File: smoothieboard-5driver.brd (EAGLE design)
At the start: 129.5 x 105.1 mm, 253 parts, among them IC1 LPC1769, IC10 LM1117-3.3V, IC11 78L12F, IC12 A4982, IC2 A4982, IC3 A4982, IC4 MCP44X1, IC5 A4982, IC6 A4982, IC9 MCP44X1, J10 POWER_JACKSMD, Q1 BSL207SP, Q2 12MHz, Q3 25MHz, Q6 AOT240L, Q7 AOT240L, Q8 ZXMN4A06GTA, Q9 ZXMN4A06GTA, U1 USD-SOCKETNEW, X14 USBPTH

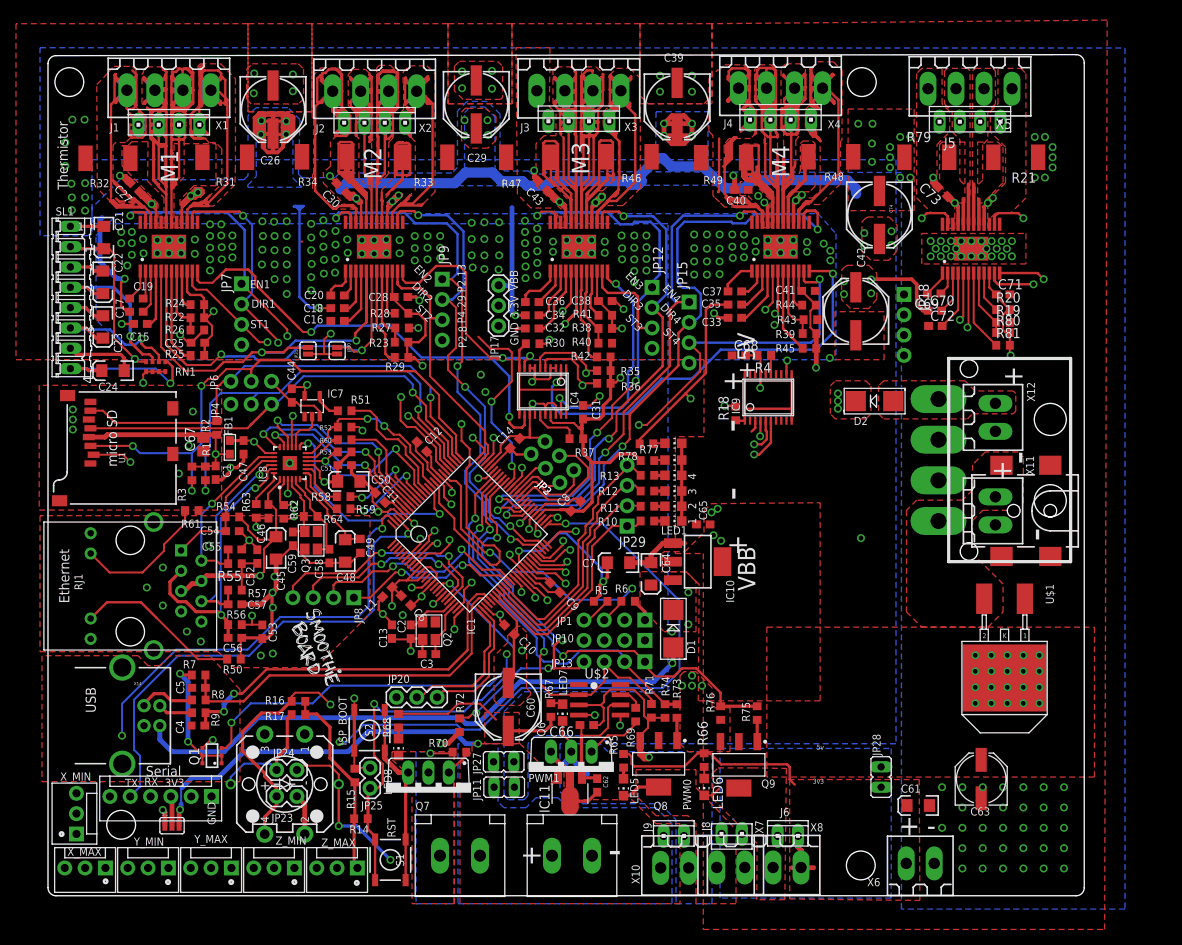
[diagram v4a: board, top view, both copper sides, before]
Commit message: remove VBB poly supplying mosfet drivers from bottom of board to improve driver heatsinking, VBB poly on route15 is adequate.
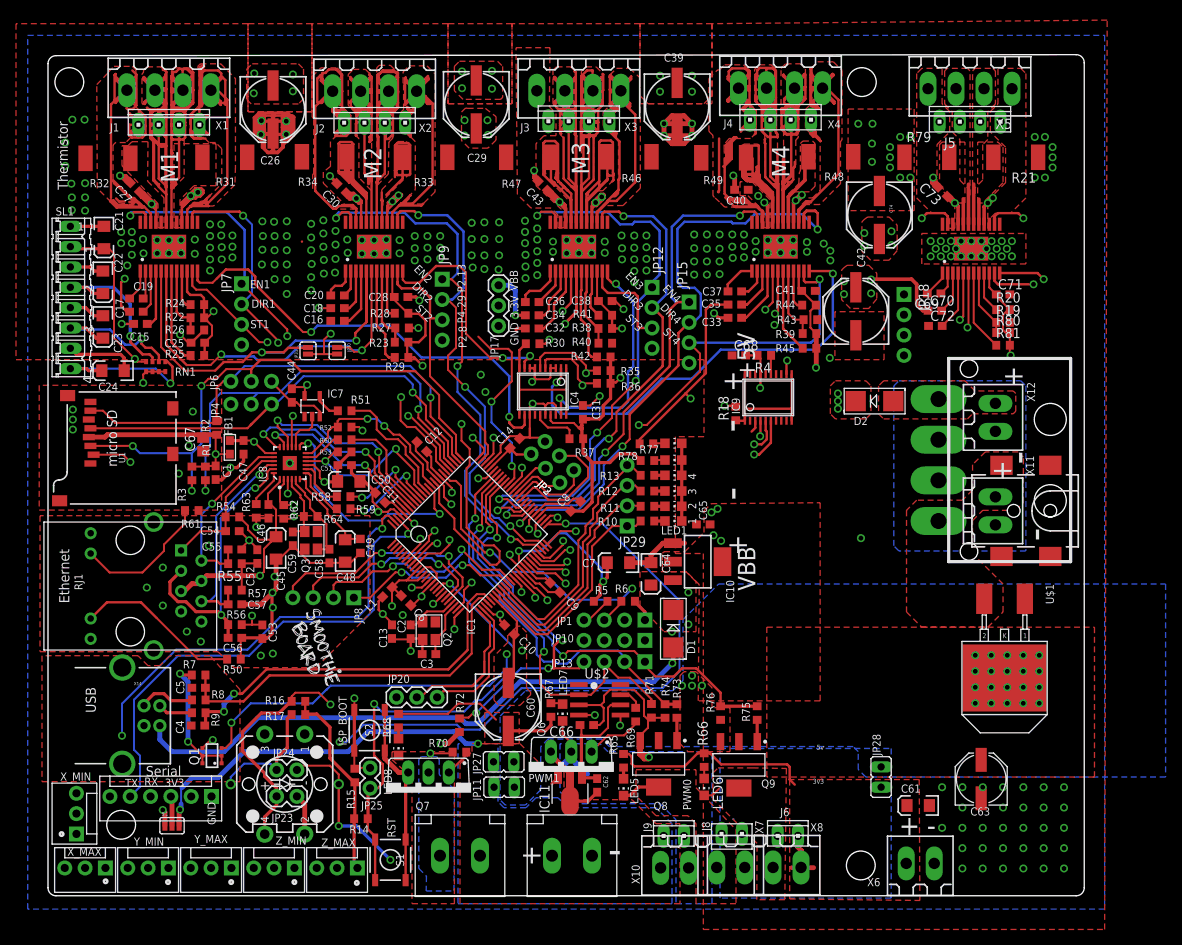
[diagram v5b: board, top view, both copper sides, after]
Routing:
- net VBB: track 351.1 -> 276.3 mm

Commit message: Gave small mosfets more heatsink area, moved some signal traces from bottom layer to route15 to improve stepper driver cooling, lots of other tweaks
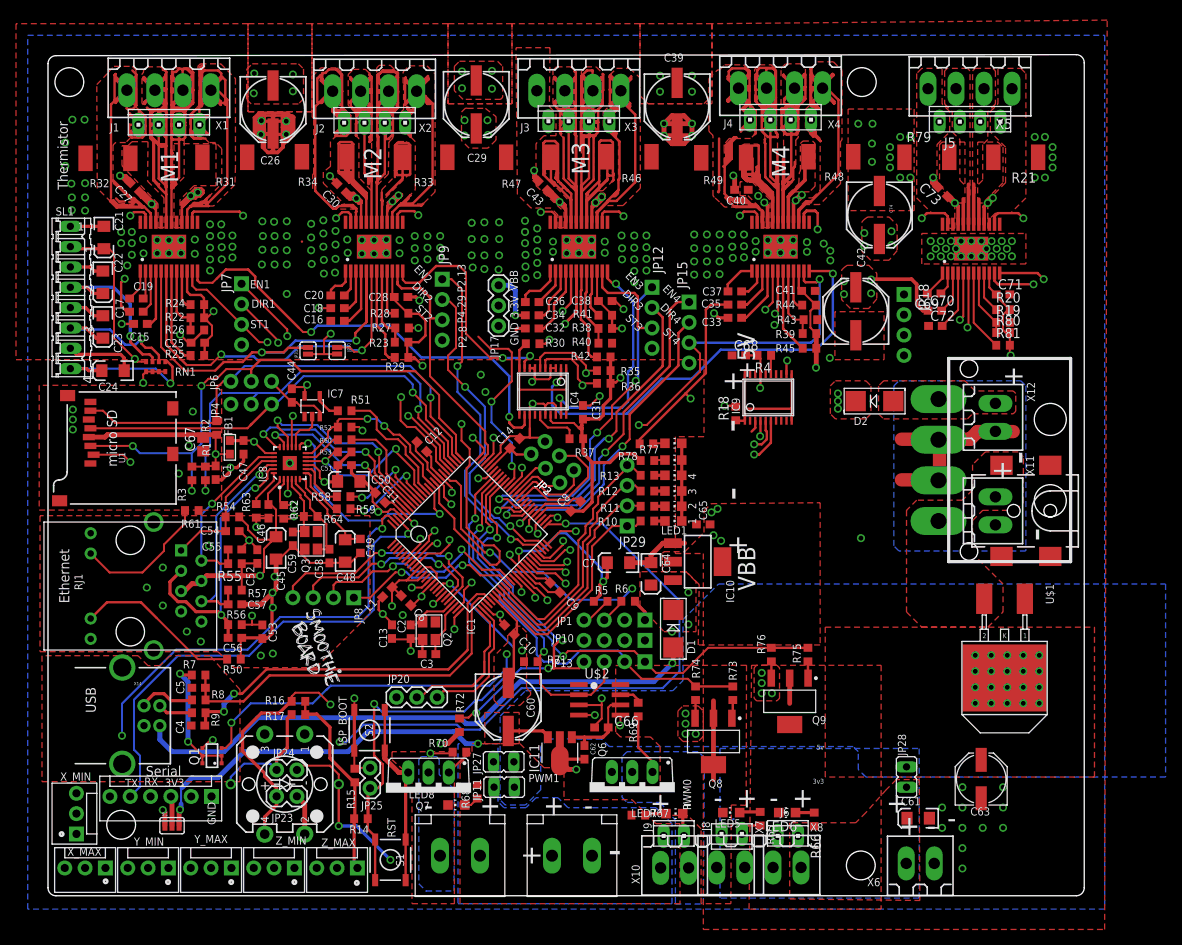
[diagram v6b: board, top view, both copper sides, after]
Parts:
- moved LED7 18.8 mm to (78.3, 9.40), turned to 270 degrees
- moved R65 18.6 mm to (89.0, 8.76), turned to 90 degrees
- moved R67 17.1 mm to (73.8, 9.21), turned to 0 degrees
- moved R71 16.3 mm to (60.4, 28.4), turned to 0 degrees
- moved R66 15.6 mm to (95.8, 8.68), turned to 90 degrees
- moved LED5 13.8 mm to (85.4, 9.53), turned to 90 degrees
- moved R68 13.3 mm to (53.7, 12.1)
- moved LED6 10.9 mm to (92.4, 9.53), turned to 90 degrees
- moved LED8 10.2 mm to (51.1, 10.5), turned to 90 degrees
- moved Q9 10.2 mm to (92.7, 23.4)
- moved R76 9.68 mm to (90.4, 29.3)
- moved R75 9.68 mm to (95.0, 29.3)
- moved Q6 8.03 mm to (73.0, 12.1)
- moved Q8 7.41 mm to (83.2, 18.4)
- moved R73 7.33 mm to (85.6, 24.4)
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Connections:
- net N$18 renamed SMALL_MOSFET_POWER
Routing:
- net SMALL_MOSFET_POWER: track 32.8 -> 3.04 mm
- net 5V: track 109.4 -> 129.7 mm
- net MOSFET_DRIVE: track 21.3 -> 5.38 mm
- net N$92: track 11.0 -> 2.86 mm
- net PWM1: track 51.5 -> 43.5 mm
- net 12VREG: track 16.6 -> 10.6 mm
- net PWM0: track 49.5 -> 55.4 mm
- net N$88: track 5.34 -> 9.84 mm
- net P2.6: track 58.0 -> 61.6 mm
- net GND: track 264.9 -> 268.1 mm, vias 300 -> 281
- net N$18: track 2.23 -> 3.81 mm
- net EN3: track 71.2 -> 70.0 mm
- net N$81: track 1.40 -> 2.61 mm
- net N$105: track 1.51 -> 2.69 mm
- net PW5: track 46.1 -> 47.2 mm
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- removed copper zone on layer 15, net 5V

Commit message: Added a bunch of ground stitching vias, also some routing tweaks
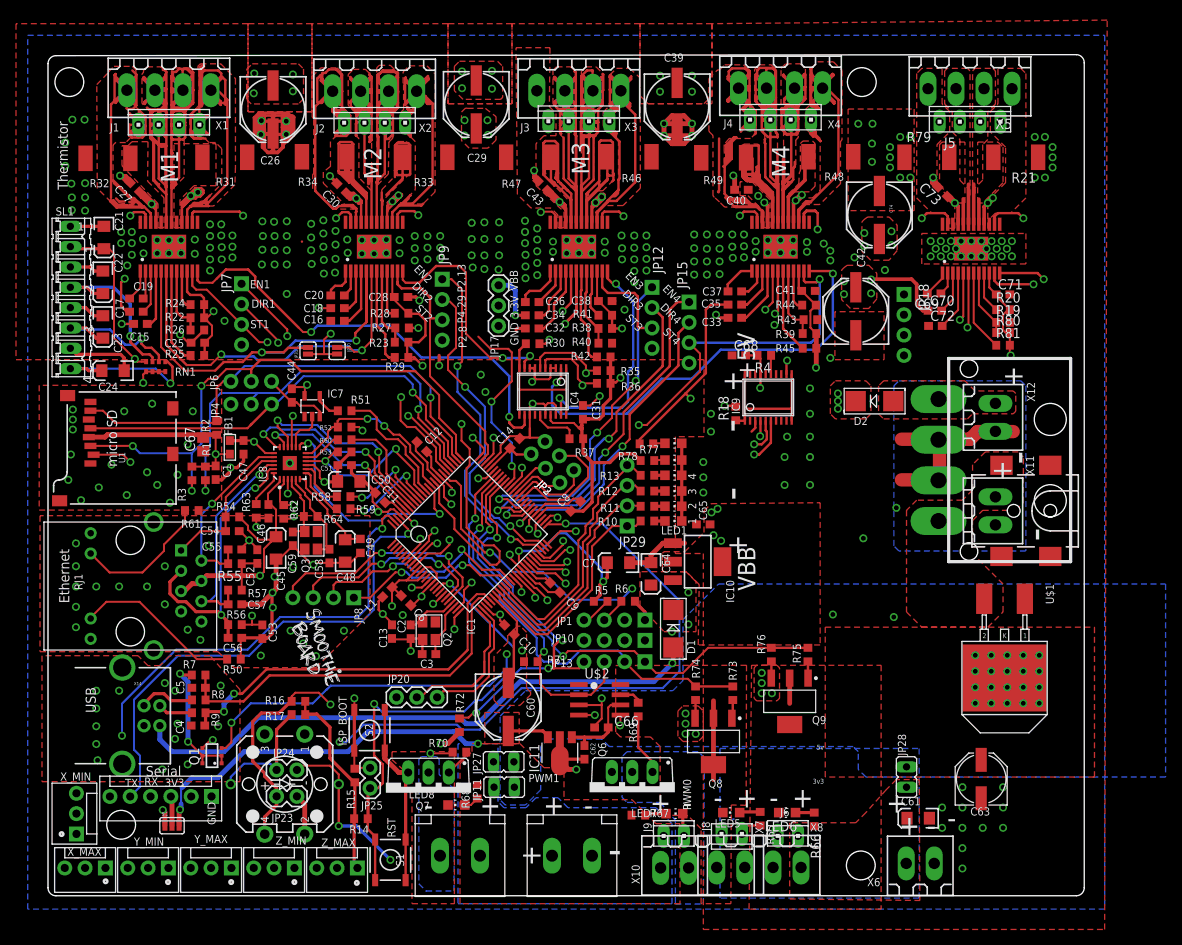
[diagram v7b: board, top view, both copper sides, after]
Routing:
- net PLAY_LED: track 123.9 -> 120.1 mm
- net X_MAX: track 83.8 -> 85.0 mm
- net PLAY: track 110.3 -> 109.3 mm
- net GND: track 268.1 -> 267.0 mm, vias 281 -> 338
